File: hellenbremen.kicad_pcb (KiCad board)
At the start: 4 copper layers, 102 x 107 mm, 52 parts, among them J2 Conn_01x03_Pin, J3 USB_C_Receptacle_USB2.0_16P, M1 Module-stlink-0.1, M2 Module-power_12and5V-0.2, M3 Module-mega-mcu144-0.6, M4 Module-vr-max9924-0.1, M5 Module-knock-0.2, M6 Module-knock-0.2, Q1 ISL9V3040D3ST, Q2 ISL9V3040D3ST, U1 RNBD451PE-I100, U2 VNLD5160TR-E, U3 VNLD5160TR-E, U4 VNLD5160TR-E

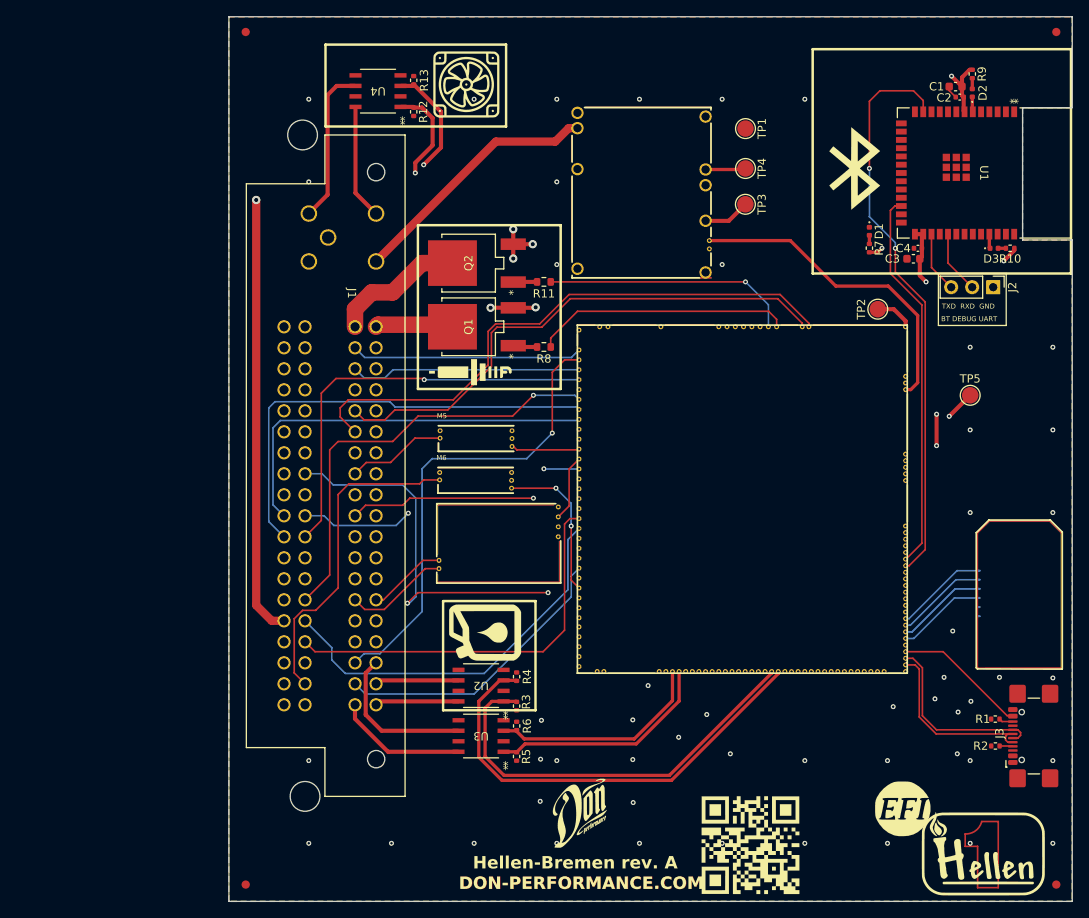
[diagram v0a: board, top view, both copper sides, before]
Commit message: adding electronic throttle control
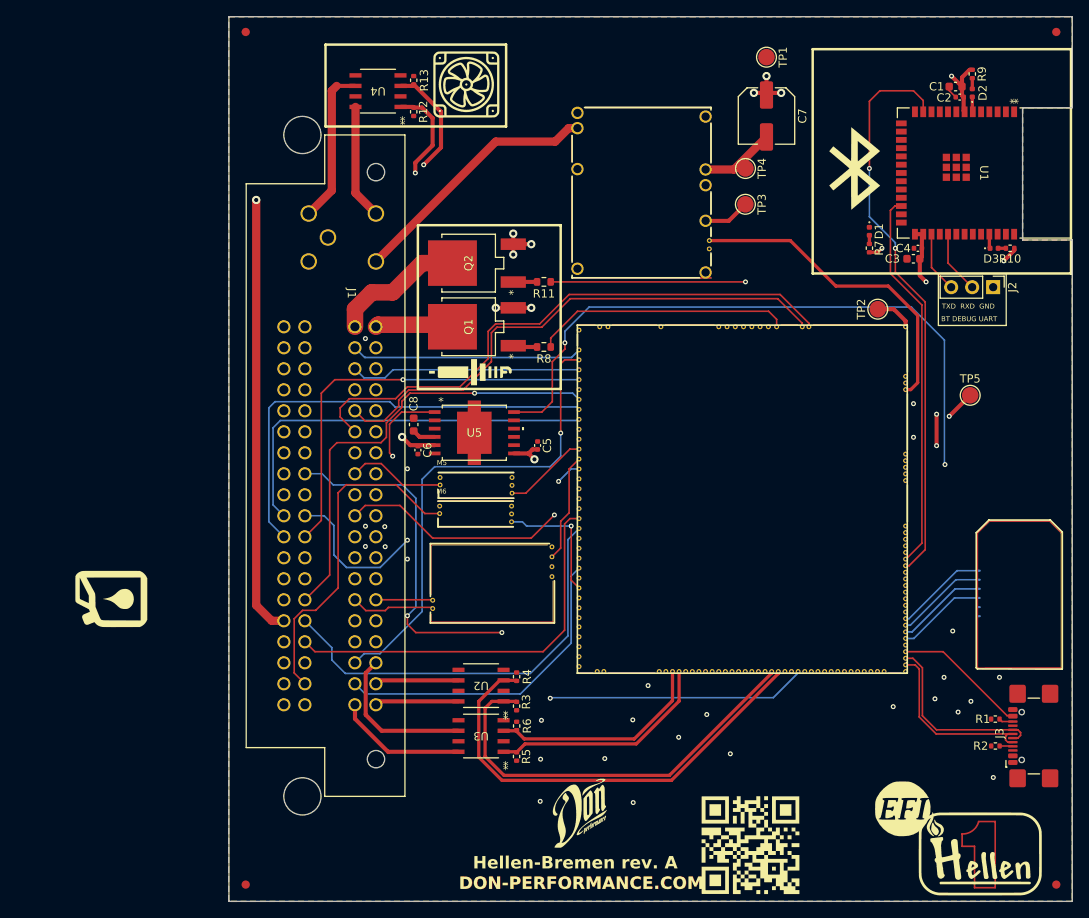
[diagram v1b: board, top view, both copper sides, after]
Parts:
- added C5: 10nF, Capacitor_SMD:C_0402_1005Metric, F.Cu at (98.3, 86.8)
- added C6: 10nF, Capacitor_SMD:C_0402_1005Metric, F.Cu at (83.8, 87.4)
- added C7: 100uF, Capacitor_SMD:C_Elec_6.3x5.8, F.Cu at (126.0, 47.0)
- added C8: 100nF, Capacitor_SMD:C_0603_1608Metric, F.Cu at (83.3, 84.3)
- added U5: TLE9201SGAUMA1, TLE9201SG:TLE9201SGAUMA1_INF, F.Cu at (90.6, 85.3)
- moved G*** 45.4 mm to (46.7, 105.4)
- moved TP1 9.00 mm to (126.0, 39.9)
- moved M5 5.66 mm to (86.2, 93.3)
- moved M4 4.89 mm to (85.2, 108.4)
- moved M6 4.06 mm to (86.2, 96.8)
- moved G*** 0.37 mm to (152.1, 136.3)
- turned FID1 to 180 degrees
- turned FID2 to 180 degrees
- turned FID3 to 0 degrees
- turned FID4 to 0 degrees
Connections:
- J1 pad 20: unconnected-(J1-ETCL-Pad20) -> ETC_OUT_M
- J1 pad 21: unconnected-(J1-ETCH-Pad21) -> ETC_OUT_P
- M3 pad E15: unconnected-(M3-OUT_PWM4-PadE15) -> ETC_DIR
- M3 pad E16: unconnected-(M3-OUT_PWM3-PadE16) -> ETC_PWM
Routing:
- net ETC_PWM: track 0.00 -> 123.1 mm, vias 0 -> 2
- net ETC_DIR: track 0.00 -> 86.6 mm, vias 0 -> 2
- net MCU_CPC: track 111.1 -> 144.3 mm
- net MCU_CFC: track 124.6 -> 154.8 mm
- net ETC_OUT_P: track 0.00 -> 26.8 mm, vias 0 -> 1
- net ETC_OUT_M: track 0.00 -> 8.83 mm, vias 0 -> 1
- net IN_MAP: track 36.5 -> 43.8 mm
- net +12V: track 4.62 -> 11.8 mm
- net ETS: track 53.5 -> 60.1 mm
- net IN_CRANK: track 8.04 -> 13.2 mm
- net MCU_KNOCK_R: track 18.6 -> 15.3 mm, vias 2 -> 1
- net H2OSPC: track 35.4 -> 38.6 mm
- net H2OS2: track 47.5 -> 50.7 mm
- net CRANK_LOW: track 9.60 -> 6.89 mm
- net GND: track 11.9 -> 14.5 mm, vias 56 -> 35
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
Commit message: adding most remaining outputs and sensors like vvt, cam etc
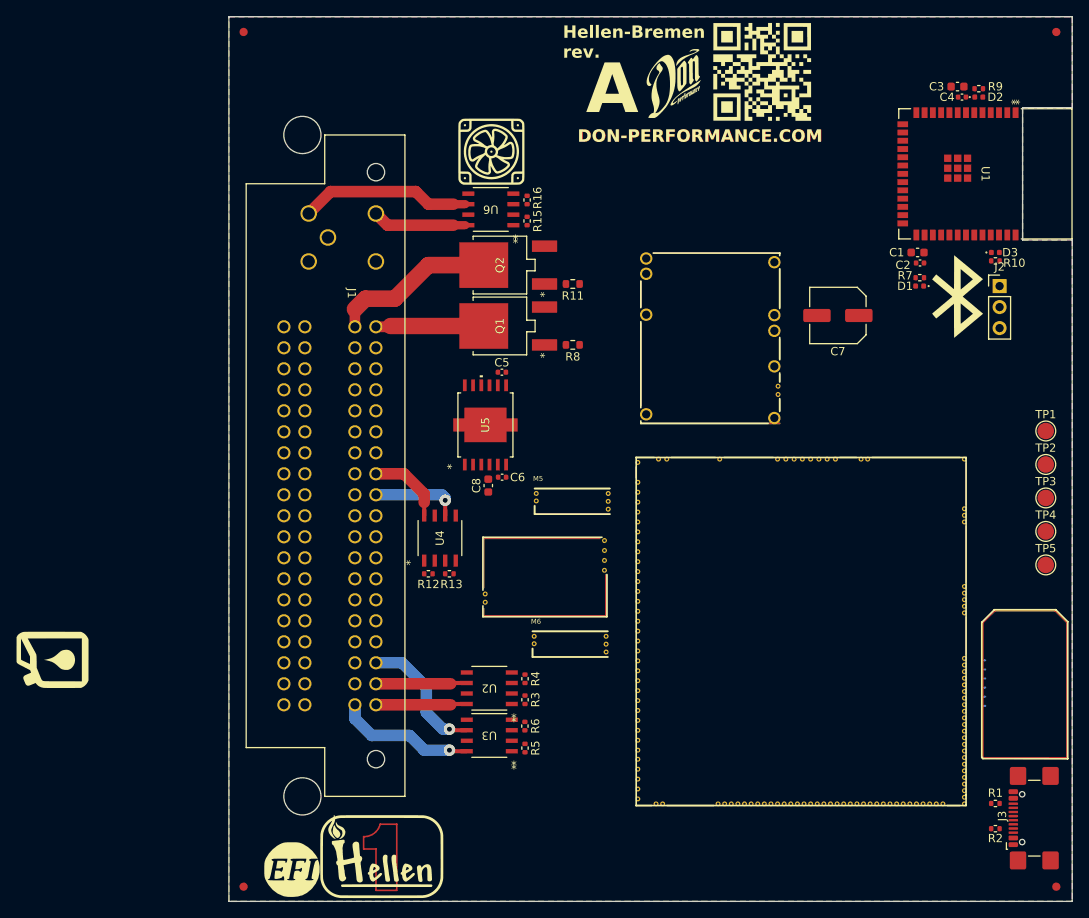
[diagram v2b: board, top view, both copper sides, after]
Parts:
- removed the G*** at (90.2, 78.0)
- added R15: 4.7k, Resistor_SMD:R_0402_1005Metric, F.Cu at (97.0, 59.7)
- added R16: 4.7k, Resistor_SMD:R_0402_1005Metric, F.Cu at (97.0, 57.2)
- added U6: VNLD5160TR-E, VNLD5160TR-E:SO_160TR-E_STM, F.Cu at (92.6, 58.3)
- moved FID4 98.3 mm to (62.7, 140.2)
- moved FID3 98.0 mm to (161.0, 140.2)
- moved G*** 93.5 mm to (125.5, 41.7)
- moved G*** 89.0 mm to (114.8, 42.9)
- moved G*** 74.2 mm to (68.6, 138.2)
- moved G*** 72.4 mm to (79.8, 136.7)
- moved R13 59.8 mm to (87.6, 102.4), turned to 0 degrees
- moved TP4 57.0 mm to (159.8, 97.2), turned to 0 degrees
- moved TP1 56.4 mm to (159.8, 85.1), turned to 0 degrees
- moved R12 55.9 mm to (85.1, 102.4), turned to 0 degrees
- moved U4 54.6 mm to (86.5, 98.0), turned to 90 degrees
- moved TP3 50.8 mm to (159.8, 93.2), turned to 0 degrees
- moved TP2 27.7 mm to (159.8, 89.1), turned to 0 degrees
- moved C7 25.6 mm to (134.6, 71.1), turned to 180 degrees
- moved TP5 22.5 mm to (159.8, 101.3)
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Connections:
- J1 pad 16: unconnected-(J1-PRGSEL-Pad16) -> PRGSEL
- J1 pad 17: unconnected-(J1-FIVVTC-Pad17) -> FIVVTC
- J1 pad 77: unconnected-(J1-FICMPSNS-Pad77) -> IN_CAM_HALL
- M3 pad E31: unconnected-(M3-OUT_INJ5-PadE31) -> MCU_PRGSEL
- M3 pad E32: unconnected-(M3-OUT_INJ6-PadE32) -> MCU_FIVVTC
- M3 pad N30: unconnected-(M3-V5A_SWITCHABLE-PadN30) -> +5VA
- M3 pad S17: IN_JSS -> unconnected-(M3-IN_RES1-PadS17)
- M3 pad S3: unconnected-(M3-IN_D2-PadS3) -> IN_CAM_HALL
- M3 pad S35: unconnected-(M3-VREF1-PadS35) -> VREF1
- M3 pad S4: unconnected-(M3-IN_D1-PadS4) -> IN_JSS
- M3 pad W2: +5VA -> unconnected-(M3-V5A_SWITCHABLE-PadW2)
- M4 pad E4: unconnected-(M4-V5_IN-PadE4) -> +5VA
- M5 pad E1: unconnected-(M5-V5A-PadE1) -> +5VA
- M5 pad W2: unconnected-(M5-VREF-PadW2) -> VREF1
- M6 pad E1: unconnected-(M6-V5A-PadE1) -> +5VA
- M6 pad W2: unconnected-(M6-VREF-PadW2) -> VREF1
- R12 pad 1: MCU_CPC -> MCU_PRGSEL
- R13 pad 1: MCU_CFC -> MCU_FIVVTC
- U4 pad 1: MCU_CPC -> MCU_PRGSEL
- U4 pad 3: MCU_CFC -> MCU_FIVVTC
- U4 pad 6: CFC -> PRGSEL
- U4 pad 8: CPC -> FIVVTC
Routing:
- net MCU_CFC: track 154.8 -> 0.00 mm, vias 1 -> 0
- net MCU_CPC: track 144.3 -> 0.00 mm, vias 1 -> 0
- net ETC_PWM: track 123.1 -> 0.00 mm, vias 2 -> 0
- net +12V_BAT: track 111.6 -> 0.00 mm, vias 1 -> 0
- net +3V3SW: track 93.0 -> 0.00 mm, vias 5 -> 0
- net ETC_DIR: track 86.6 -> 0.00 mm, vias 2 -> 0
- net CAN_L: track 69.8 -> 0.00 mm
- net UART_BT_TX: track 69.1 -> 0.00 mm, vias 2 -> 0
- net CAN_H: track 64.9 -> 0.00 mm
- net ETS: track 60.1 -> 0.00 mm, vias 2 -> 0
- net IN_TPS2: track 58.2 -> 0.00 mm, vias 1 -> 0
- net MCU_INJ2: track 55.4 -> 0.00 mm
- net VIGN: track 54.6 -> 0.00 mm, vias 2 -> 0
- net IN_AAT: track 54.6 -> 0.00 mm
- net IN_CLT: track 54.1 -> 0.00 mm, vias 1 -> 0
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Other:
- board text added: "A"
- board text added: "Hellen-Bremen rev."
- board text removed: "BT DEBUG UART"
- board text removed: "Hellen-Bremen rev. A"
- board text removed: "TXD RXD GND"

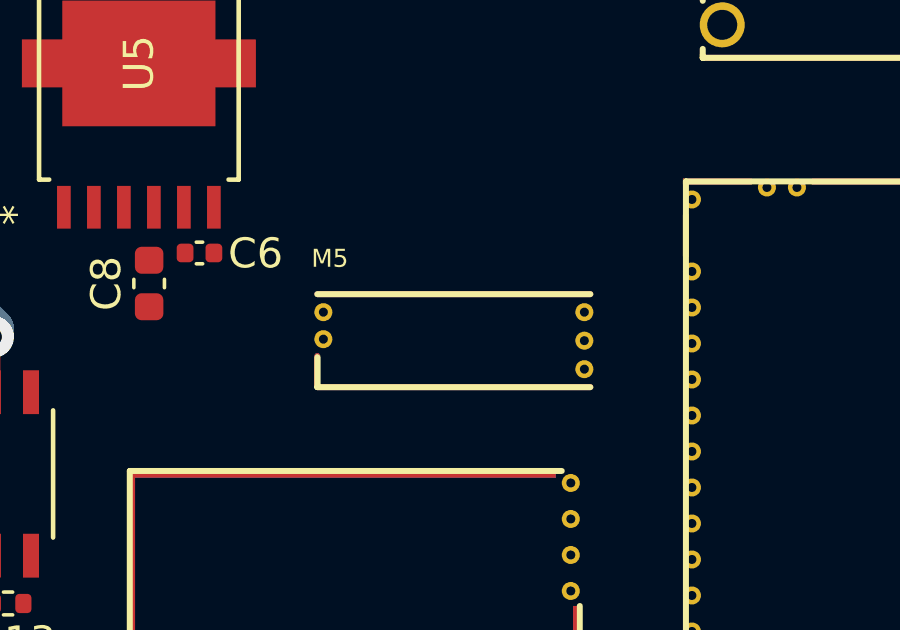
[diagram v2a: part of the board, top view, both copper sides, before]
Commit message: J1 not in BOM
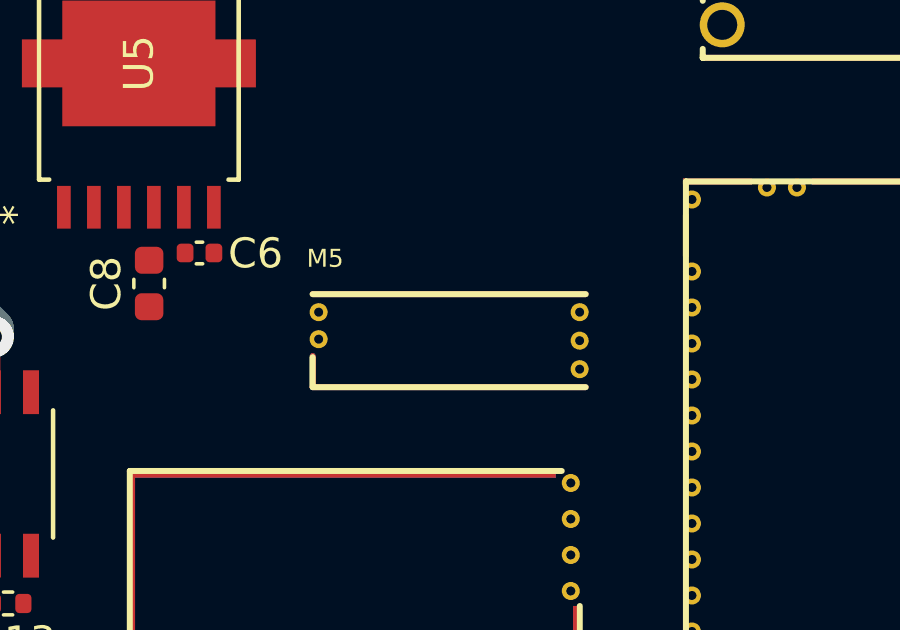
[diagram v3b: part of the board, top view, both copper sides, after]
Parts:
- moved M5 0.16 mm to (97.7, 95.3)
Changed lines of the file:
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@@
 	(footprint "hellen_knock:knock"
 		(layer "F.Cu")
-		(at 97.837 95.251002)
+		(at 97.68 95.251002)
 		(property "Reference" "M5"
 			(at -0.0998 -4.0382 0)
@@
 			(polygon
 				(pts
-					(xy 107.037 95.151002) (xy 97.937 95.151002) (xy 97.937 92.050999) (xy 107.037 92.050999)
+					(xy 106.88 95.151002) (xy 97.78 95.151002) (xy 97.78 92.050999) (xy 106.88 92.050999)
 				)
 			)
@@
 		(sheetname "Root")
 		(sheetfile "hellenbremen.kicad_sch")
-		(attr through_hole exclude_from_bom)
+		(attr through_hole exclude_from_pos_files exclude_from_bom)
 		(fp_line
 			(start -17.3 7.1)

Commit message: redone layout, possibly feature complete
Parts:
- removed the G*** at (39.6, 112.8)
- removed U5: TLE9201SGAUMA1, TLE9201SG:TLE9201SGAUMA1_INF
- added IC1: TLE9201SG, TLE9201SG:TLE9201SG, B.Cu at (89.4, 83.5)
- added R17: 4.7k, Resistor_SMD:R_0402_1005Metric, F.Cu at (94.2, 84.1)
- added R18: 4.7k, Resistor_SMD:R_0402_1005Metric, F.Cu at (93.7, 81.5)
- added R19: 4.7k, Resistor_SMD:R_0402_1005Metric, F.Cu at (95.0, 128.7)
- added R20: 4.7k, Resistor_SMD:R_0402_1005Metric, F.Cu at (93.8, 126.1)
- added U7: VNLD5160TR-E, VNLD5160TR-E:SO_160TR-E_STM, F.Cu at (89.4, 82.8)
- added U8: VNLD5160TR-E, VNLD5160TR-E:SO_160TR-E_STM, F.Cu at (89.4, 127.3)
- C5, C6, C8: moved to B.Cu
- moved TP4 51.3 mm to (129.8, 55.6)
- moved TP3 38.3 mm to (131.8, 67.1)
- moved M1 23.9 mm to (148.8, 130.3), turned to 180 degrees
- moved TP2 23.1 mm to (139.7, 77.7)
- moved TP5 20.9 mm to (159.8, 80.4)
- moved R13 14.0 mm to (93.7, 89.8), turned to 90 degrees
- moved R12 13.7 mm to (94.5, 92.3), turned to 90 degrees
- moved C6 11.3 mm to (82.8, 88.9), turned to 180 degrees
- moved C7 10.7 mm to (132.3, 60.7)
- moved M2 10.3 mm to (110.0, 74.0)
- moved M3 8.13 mm to (112.2, 80.3)
- moved U4 7.69 mm to (89.4, 90.9), turned to 180 degrees
- moved C5 6.87 mm to (87.3, 76.2), turned to 180 degrees
- moved G*** 5.39 mm to (120.1, 43.7)
- moved C8 5.25 mm to (87.1, 92.5), turned to 0 degrees
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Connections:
- J1 pad 14: GND -> FHO2H
- J1 pad 23: GND -> RHO2H
- J1 pad 31: unconnected-(J1-FLS-Pad31) -> FLS
- J1 pad 44: unconnected-(J1-CFFC-Pad44) -> CCFC
- J1 pad 78: unconnected-(J1-GEARSENS-Pad78) -> GEAR_POS_SENS
- J1 pad 80: unconnected-(J1-PCHO2SHTR-Pad80) -> PCHO2SHTR
- M2 pad V3: +12V_BAT -> +12V_PSP
- M3 pad E14: unconnected-(M3-OUT_PWM5-PadE14) -> MCU_CCFC
- M3 pad E26: unconnected-(M3-OUT_PWM6-PadE26) -> MCU_PCHO2SHTR
- M3 pad E29: unconnected-(M3-OUT_INJ3-PadE29) -> MCU_FHO2H
- M3 pad E30: unconnected-(M3-OUT_INJ4-PadE30) -> MCU_RHO2H
- M3 pad N22: +3V3 -> unconnected-(M3-V33-PadN22)
- M3 pad N30: +5VA -> unconnected-(M3-V5A_SWITCHABLE-PadN30)
- M3 pad S13: ETS -> unconnected-(M3-IN_AUX1-PadS13)
- M3 pad S5: unconnected-(M3-VREF2-PadS5) -> VREF2
- M3 pad S6: unconnected-(M3-IN_SENS4-PadS6) -> GEAR_POS_SENS
- M3 pad S7: unconnected-(M3-IN_SENS3-PadS7) -> FLS
- M3 pad S8: unconnected-(M3-IN_SENS2-PadS8) -> ETS
- M3 pad W10: MCUIGN_2 -> MCUIGN_1
- M3 pad W11: MCUIGN_1 -> MCUIGN_2
- M3 pad W2: unconnected-(M3-V5A_SWITCHABLE-PadW2) -> +5VA
- M6 pad W2: VREF1 -> VREF2
- R3 pad 1: MCU_INJ1 -> MCU_INJ2
- R4 pad 1: MCU_INJ2 -> MCU_ACR2
- R6 pad 1: MCU_ACR2 -> MCU_INJ1
- U2 pad 1: MCU_INJ1 -> MCU_INJ2
- U2 pad 3: MCU_INJ2 -> MCU_ACR2
- U2 pad 6: INJ_2 -> ACR_2
- U2 pad 8: INJ_1 -> INJ_2
- U3 pad 3: MCU_ACR2 -> MCU_INJ1
- U3 pad 6: ACR_2 -> INJ_1
- U4 pad 6: PRGSEL -> FIVVTC
- U4 pad 8: FIVVTC -> PRGSEL
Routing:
- net +3V3SW: track 0.00 -> 119.7 mm, vias 0 -> 6
- net MCU_CFC: track 0.00 -> 111.9 mm, vias 0 -> 1
- net MCU_CPC: track 0.00 -> 102.4 mm, vias 0 -> 1
- net +12V_BAT: track 0.00 -> 102.0 mm
- net MCU_PCHO2SHTR: track 0.00 -> 97.3 mm, vias 0 -> 4
- net ETC_PWM: track 0.00 -> 95.6 mm
- net GEAR_POS_SENS: track 0.00 -> 92.9 mm, vias 0 -> 2
- net ETC_DIR: track 0.00 -> 89.0 mm
- net IN_CAM_HALL: track 0.00 -> 87.9 mm, vias 0 -> 1
- net UART_BT_TX: track 0.00 -> 85.6 mm
- net MCU_RHO2H: track 0.00 -> 83.3 mm, vias 0 -> 3
- net MCU_PRGSEL: track 0.00 -> 76.1 mm, vias 0 -> 2
- net +3V3: track 0.00 -> 74.5 mm, vias 0 -> 2
- net MCU_FIVVTC: track 0.00 -> 74.1 mm, vias 0 -> 2
- net +12V: track 0.00 -> 74.0 mm, vias 0 -> 2
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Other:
- board text added: "WWW.DON-PERFORMANCE.COM"
- board text removed: "DON-PERFORMANCE.COM"

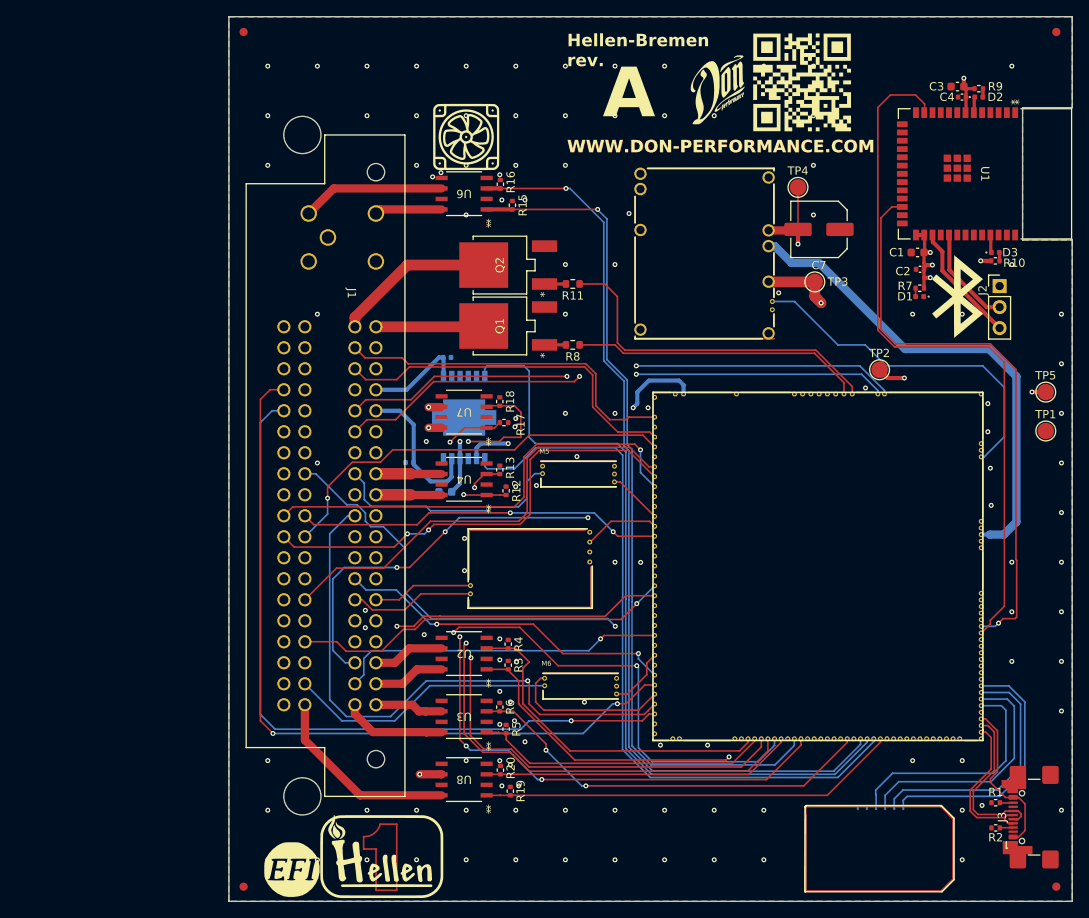
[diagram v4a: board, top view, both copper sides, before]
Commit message: Proper stronger mosfet for coolant fan and pump
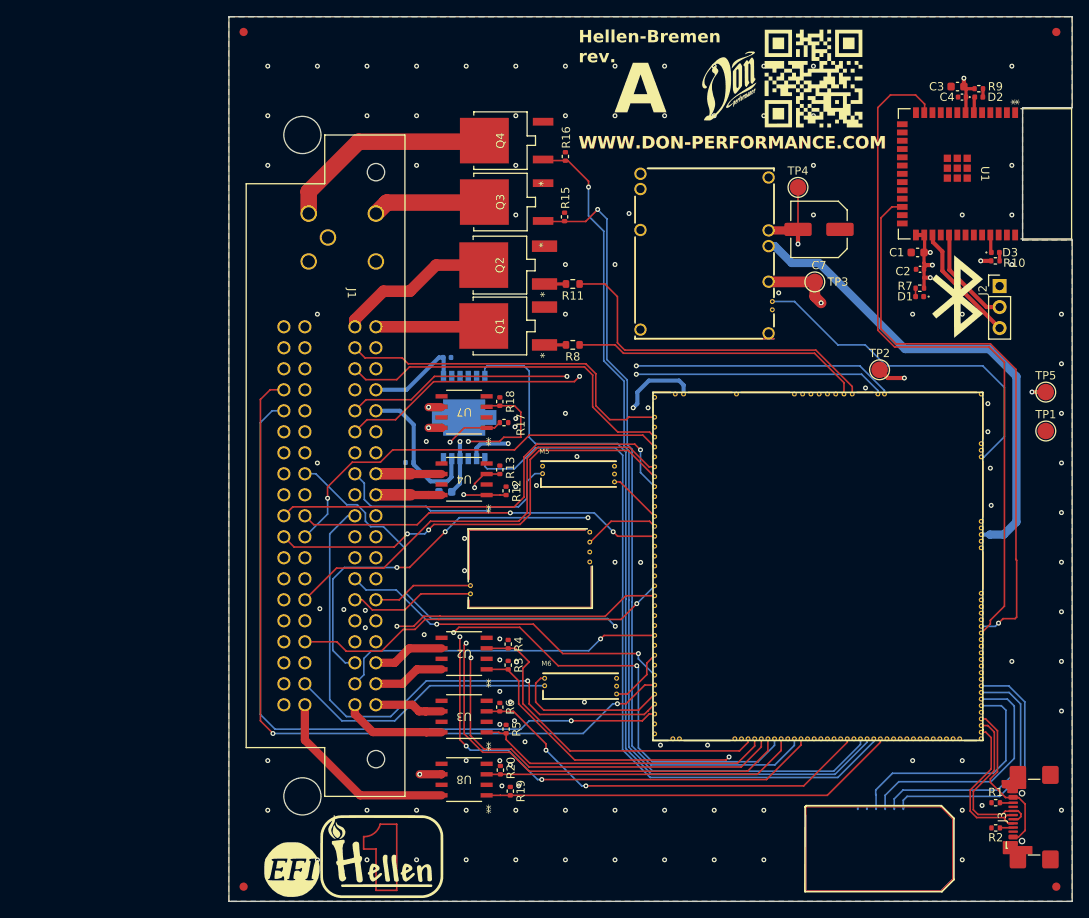
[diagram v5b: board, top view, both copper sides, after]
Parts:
- removed the G*** at (89.7, 49.5)
- removed U6: VNLD5160TR-E, VNLD5160TR-E:SO_160TR-E_STM
- added Q3: DMN6040SK3-13, DMN6040SK3_13:D-PAK_DMN6040SK3-13_DIO, F.Cu at (93.8, 57.4)
- added Q4: DMN6040SK3-13, DMN6040SK3_13:D-PAK_DMN6040SK3-13_DIO, F.Cu at (93.8, 50.0)
- moved R16 8.55 mm to (101.7, 51.9)
- moved R15 6.47 mm to (101.6, 59.2)
- moved G*** 1.46 mm to (121.5, 43.2)
- moved G*** 1.46 mm to (131.7, 42.5)
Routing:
- net CFC: track 17.3 -> 26.4 mm
- net MCU_CPC: track 102.4 -> 96.2 mm
- net CPC: track 8.15 -> 13.7 mm
- net MCU_CFC: track 111.9 -> 108.3 mm
- net MCU_FHO2H: track 37.7 -> 38.2 mm
- net GND: vias 124 -> 118
